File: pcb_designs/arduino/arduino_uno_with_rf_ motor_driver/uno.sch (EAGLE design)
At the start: 28 parts, among them IC1 ATMEGA328, IC2 7805, IC3 L293D, Q1 16MHZ

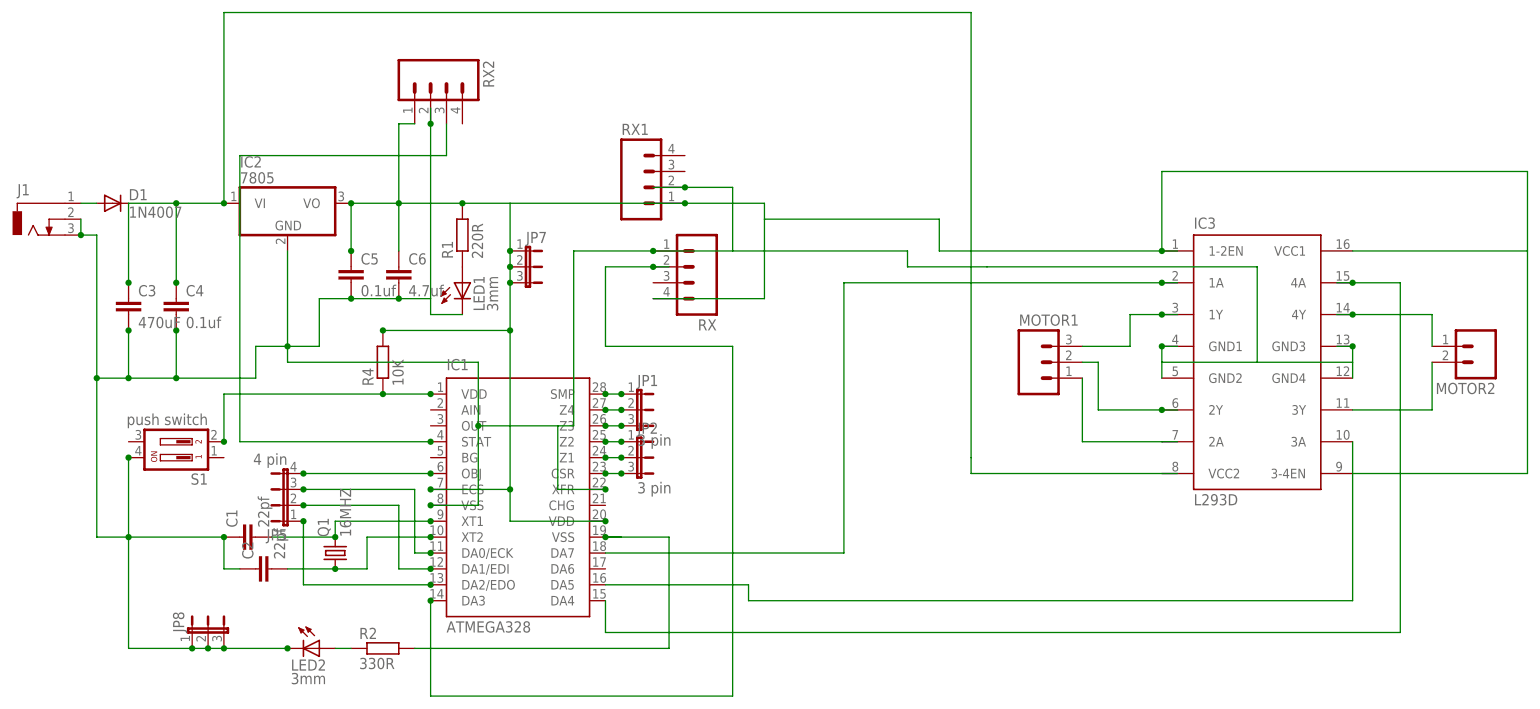
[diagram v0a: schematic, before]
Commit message: change arduino interfacing with rf and motor driver
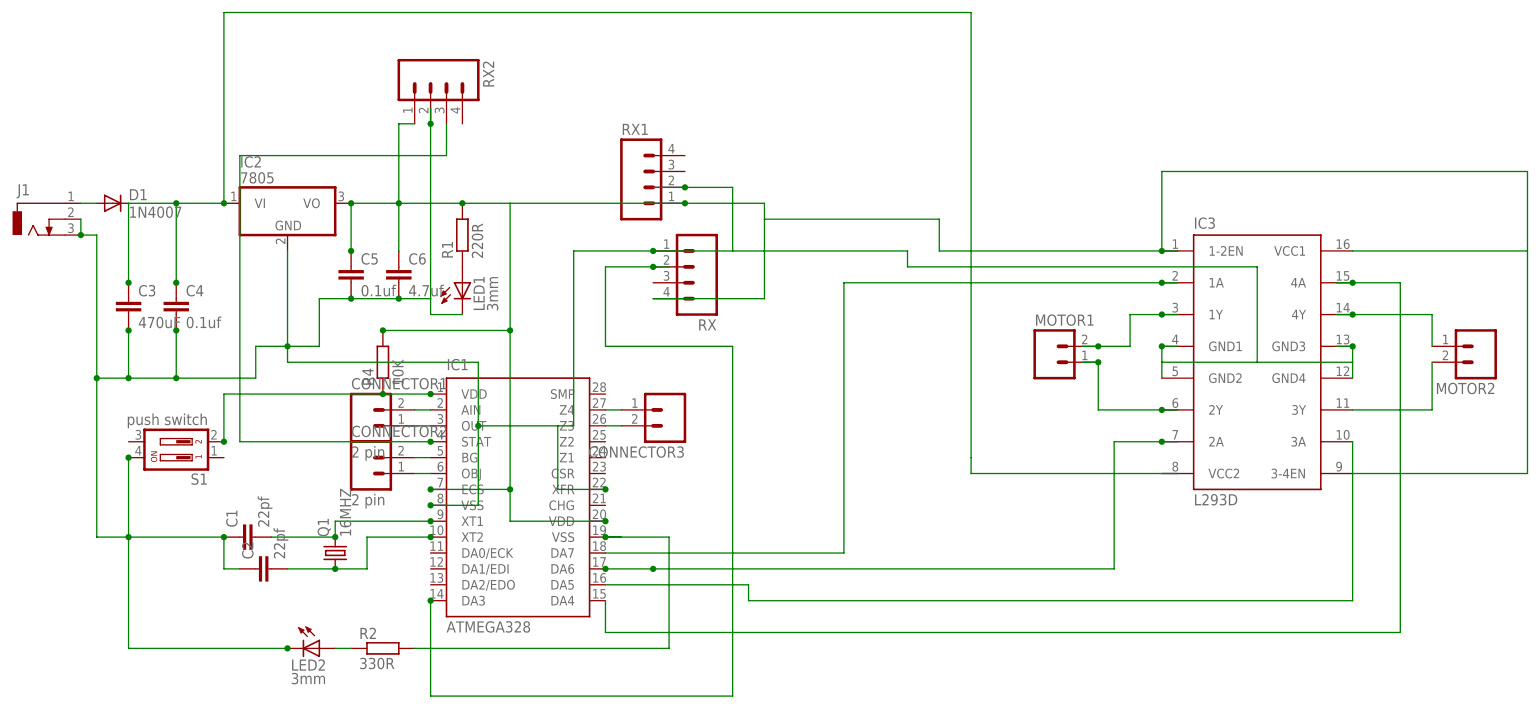
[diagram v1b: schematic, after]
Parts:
- removed JP1, JP2: 3 pin, jumper:JP2E
- removed JP5: 4 pin, jumper:JP4E
- removed JP7, JP8: (no value), jumper:JP2E
- added CONNECTOR1, CONNECTOR2: 2 pin, con-amp-quick:M02
- added CONNECTOR3: (no value), con-amp-quick:M02
- MOTOR1: device con-amp-quick:M03 -> con-amp-quick:M02; OC_FARNELL (none) -> unknown; OC_NEWARK (none) -> unknown
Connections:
- removed net N$18: IC1.OBJ, JP5.4
- removed net N$19: IC1.DA1/EDI, JP5.2
- removed net N$20: IC1.DA0/ECK, JP5.3
- removed net N$29: IC1.DA2/EDO, JP5.1
- net N$10: now also CONNECTOR2.1, IC1.OBJ; no longer IC1.Z3, JP1.3
- net N$11: now also CONNECTOR2.2, IC1.BG; no longer IC1.Z2, JP2.1
- net N$12: now also CONNECTOR3.1, IC1.Z4; no longer IC1.Z1, JP2.2
- net N$13: now also CONNECTOR3.2, IC1.Z3; no longer IC1.CSR, JP2.3
- net N$33: no longer JP7.1, JP7.2, JP7.3
- net N$34: now also MOTOR1.1; no longer MOTOR1.2
- net N$35: now also MOTOR1.2; no longer MOTOR1.3
- net N$5: no longer JP8.1, JP8.2, JP8.3
- net N$7: now also IC1.DA6; no longer MOTOR1.1
- net N$8: now also CONNECTOR1.1, IC1.OUT; no longer IC1.SMP, JP1.1
- net N$9: now also CONNECTOR1.2, IC1.AIN; no longer IC1.Z4, JP1.2
